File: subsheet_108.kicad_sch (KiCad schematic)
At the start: 15 parts

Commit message: fini eprom, réarrange la feuille, version alpha
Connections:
- net ~{CS_EPROM}: now reaches I14.4 (1Y3), I14.5 (1Y2), R30.2
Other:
- note added: "Vers I04"
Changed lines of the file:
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@@
     (title "Conversion du Thomson MO5 — Unité centrale v1")
     (date "2023-05-24")
-    (rev "DRAFT")
+    (rev "ALPHA")
     (comment 1 "http://github.com/sporniket/kicad-conversions--thomson-mo5--v1")
     (comment 3 "Gate Array Motorola MCA 1300 ALS")
@@
   (junction (at 151.13 167.64) (diameter 0) (color 0 0 0 0)
   )
+  (junction (at 52.07 147.32) (diameter 0) (color 0 0 0 0)
+  )
   (junction (at 93.98 190.5) (diameter 0) (color 0 0 0 0)
   )
@@
     (stroke (width 0) (type default) (color 0 0 0 0))
   )
+  (wire (pts (xy 49.53 147.32) (xy 52.07 147.32))
+    (stroke (width 0) (type default) (color 0 0 0 0))
+  )
   (wire (pts (xy 93.98 68.58) (xy 109.22 68.58))
     (stroke (width 0) (type default) (color 0 0 0 0))
+  )
+  (text "Vers I04" (at 36.83 148.59 180)
+    (effects (font (size 1.27 1.27)) (justify right bottom))
   )
   (label "A15" (at 80.01 129.54 0)
@@
       (effects (font (size 1.27 1.27)) (justify right) hide)
     )
+  )
+  (global_label "~{CS_EPROM}" (shape output) (at 49.53 147.32 180) (fields_autoplaced)
+    (effects (font (size 1.27 1.27)) (justify right))
+    (property "Intersheet References" "${INTERSHEET_REFS}" (id 0) (at 37.1988 147.2406 0)
+      (effects (font (size 1.27 1.27)) (justify right) hide)
+    )

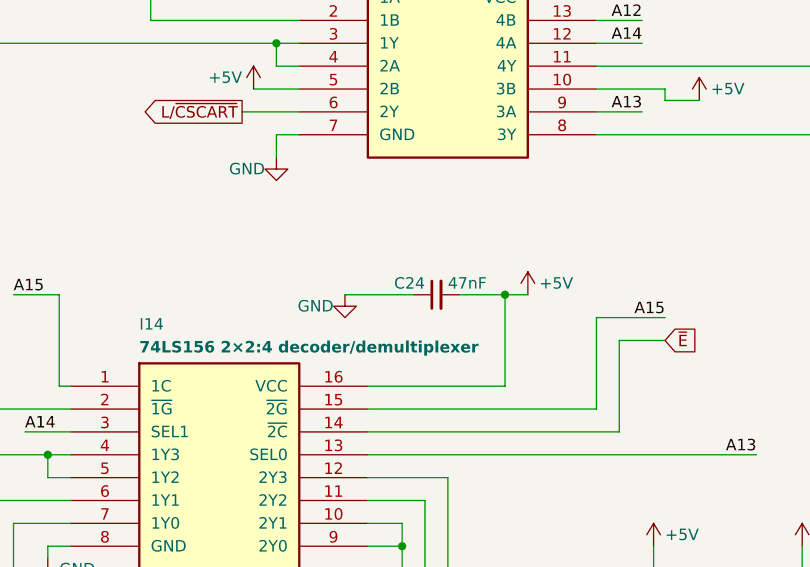
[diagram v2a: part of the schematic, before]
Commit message: fixes DRC : duplicate, designators with '?'
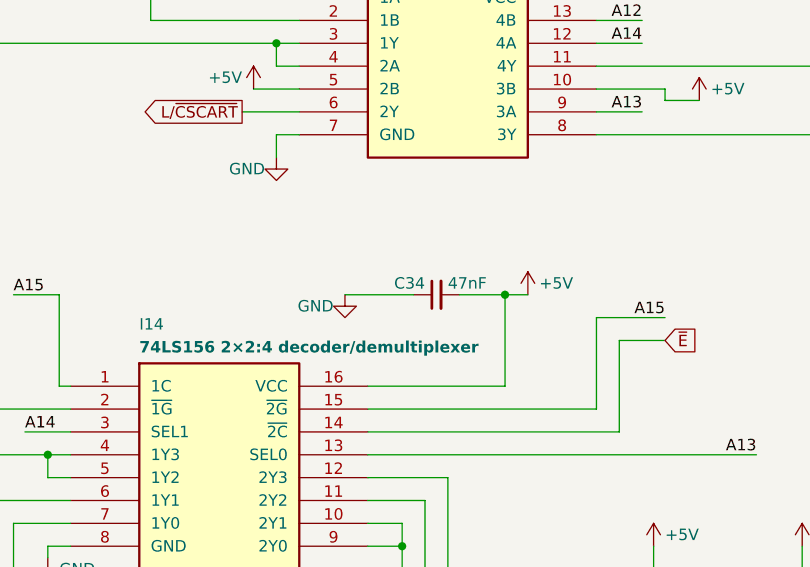
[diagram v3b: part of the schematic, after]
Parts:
- renumbered C24 to C34
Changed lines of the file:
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@@
   (symbol (lib_id "power:+5V") (at 69.85 205.74 0) (unit 1)
     (in_bom yes) (on_board yes)
-    (property "Reference" "#PWR?" (id 0) (at 69.85 209.55 0)
+    (property "Reference" "#PWR0120" (id 0) (at 69.85 209.55 0)
       (effects (font (size 1.27 1.27)) hide)
     )
@@
   (symbol (lib_id "power:GND") (at 58.42 76.2 0) (unit 1)
     (in_bom yes) (on_board yes)
-    (property "Reference" "#PWR?" (id 0) (at 58.42 82.55 0)
+    (property "Reference" "#PWR0131" (id 0) (at 58.42 82.55 0)
       (effects (font (size 1.27 1.27)) hide)
     )
@@
   (symbol (lib_id "Device:C_Small") (at 127 129.54 90) (unit 1)
     (in_bom yes) (on_board yes)
-    (property "Reference" "C24" (id 0) (at 125.73 128.27 90)
+    (property "Reference" "C34" (id 0) (at 125.73 128.27 90)
       (effects (font (size 1.27 1.27)) (justify left))
     )
@@
   (symbol (lib_id "power:+5V") (at 156.21 86.36 0) (unit 1)
     (in_bom yes) (on_board yes)
-    (property "Reference" "#PWR?" (id 0) (at 156.21 90.17 0)
+    (property "Reference" "#PWR0123" (id 0) (at 156.21 90.17 0)
       (effects (font (size 1.27 1.27)) hide)
     )
@@
   (symbol (lib_id "power:GND") (at 104.14 233.68 0) (unit 1)
     (in_bom yes) (on_board yes)
-    (property "Reference" "#PWR?" (id 0) (at 104.14 240.03 0)
+    (property "Reference" "#PWR0121" (id 0) (at 104.14 240.03 0)
       (effects (font (size 1.27 1.27)) hide)
     )
@@
   (symbol (lib_id "power:GND") (at 109.22 114.3 0) (unit 1)
     (in_bom yes) (on_board yes)
-    (property "Reference" "#PWR?" (id 0) (at 109.22 120.65 0)
+    (property "Reference" "#PWR0129" (id 0) (at 109.22 120.65 0)
       (effects (font (size 1.27 1.27)) hide)
     )
@@
   (symbol (lib_id "power:+5V") (at 106.68 106.68 0) (unit 1)
     (in_bom yes) (on_board yes)
-    (property "Reference" "#PWR?" (id 0) (at 106.68 110.49 0)
+    (property "Reference" "#PWR0119" (id 0) (at 106.68 110.49 0)
       (effects (font (size 1.27 1.27)) hide)
     )
@@
   (symbol (lib_id "power:GND") (at 116.84 129.54 0) (unit 1)
     (in_bom yes) (on_board yes)
-    (property "Reference" "#PWR?" (id 0) (at 116.84 135.89 0)
+    (property "Reference" "#PWR0130" (id 0) (at 116.84 135.89 0)
       (effects (font (size 1.27 1.27)) hide)
     )
@@
   (symbol (lib_id "power:+5V") (at 52.07 139.7 0) (unit 1)
     (in_bom yes) (on_board yes)
-    (property "Reference" "#PWR?" (id 0) (at 52.07 143.51 0)
+    (property "Reference" "#PWR0118" (id 0) (at 52.07 143.51 0)
       (effects (font (size 1.27 1.27)) hide)
     )
@@
   (symbol (lib_id "power:GND") (at 83.82 48.26 0) (unit 1)
     (in_bom yes) (on_board yes)
-    (property "Reference" "#PWR?" (id 0) (at 83.82 54.61 0)
+    (property "Reference" "#PWR0132" (id 0) (at 83.82 54.61 0)
       (effects (font (size 1.27 1.27)) hide)
     )
@@
   (symbol (lib_id "power:GND") (at 148.59 205.74 0) (unit 1)
     (in_bom yes) (on_board yes)
-    (property "Reference" "#PWR?" (id 0) (at 148.59 212.09 0)
+    (property "Reference" "#PWR0122" (id 0) (at 148.59 212.09 0)
       (effects (font (size 1.27 1.27)) hide)
     )
@@
   (symbol (lib_id "power:GND") (at 109.22 77.47 0) (unit 1)
     (in_bom yes) (on_board yes)
-    (property "Reference" "#PWR?" (id 0) (at 109.22 83.82 0)
+    (property "Reference" "#PWR0126" (id 0) (at 109.22 83.82 0)
       (effects (font (size 1.27 1.27)) hide)
     )
@@
   (symbol (lib_id "power:GND") (at 49.53 205.74 0) (unit 1)
     (in_bom yes) (on_board yes)
-    (property "Reference" "#PWR?" (id 0) (at 49.53 212.09 0)
+    (property "Reference" "#PWR0136" (id 0) (at 49.53 212.09 0)
       (effects (font (size 1.27 1.27)) hide)
     )
@@
   (symbol (lib_id "power:+5V") (at 104.14 48.26 0) (unit 1)
     (in_bom yes) (on_board yes)
-    (property "Reference" "#PWR?" (id 0) (at 104.14 52.07 0)
+    (property "Reference" "#PWR0127" (id 0) (at 104.14 52.07 0)
       (effects (font (size 1.27 1.27)) hide)
     )
@@
   (symbol (lib_id "power:GND") (at 135.89 86.36 0) (unit 1)
     (in_bom yes) (on_board yes)
-    (property "Reference" "#PWR?" (id 0) (at 135.89 92.71 0)
+    (property "Reference" "#PWR0125" (id 0) (at 135.89 92.71 0)
       (effects (font (size 1.27 1.27)) hide)
     )
@@
   (symbol (lib_id "power:GND") (at 27.94 233.68 0) (unit 1)
     (in_bom yes) (on_board yes)
-    (property "Reference" "#PWR?" (id 0) (at 27.94 240.03 0)
+    (property "Reference" "#PWR0135" (id 0) (at 27.94 240.03 0)
       (effects (font (size 1.27 1.27)) hide)
     )
@@
   (symbol (lib_id "power:+5V") (at 137.16 129.54 0) (unit 1)
     (in_bom yes) (on_board yes)
-    (property "Reference" "#PWR?" (id 0) (at 137.16 133.35 0)
+    (property "Reference" "#PWR0128" (id 0) (at 137.16 133.35 0)
       (effects (font (size 1.27 1.27)) hide)
     )
@@
   (symbol (lib_id "power:+5V") (at 167.64 157.48 0) (unit 1)
     (in_bom yes) (on_board yes)
-    (property "Reference" "#PWR?" (id 0) (at 167.64 161.29 0)
+    (property "Reference" "#PWR0139" (id 0) (at 167.64 161.29 0)
       (effects (font (size 1.27 1.27)) hide)
     )
@@
   (symbol (lib_id "power:+5V") (at 128.27 205.74 0) (unit 1)
     (in_bom yes) (on_board yes)
-    (property "Reference" "#PWR?" (id 0) (at 128.27 209.55 0)
+    (property "Reference" "#PWR0137" (id 0) (at 128.27 209.55 0)
       (effects (font (size 1.27 1.27)) hide)
     )
@@
   (symbol (lib_id "power:GND") (at 83.82 158.75 0) (unit 1)
     (in_bom yes) (on_board yes)
-    (property "Reference" "#PWR?" (id 0) (at 83.82 165.1 0)
+    (property "Reference" "#PWR0134" (id 0) (at 83.82 165.1 0)
       (effects (font (size 1.27 1.27)) hide)
     )
@@
   (symbol (lib_id "power:+5V") (at 156.21 107.95 0) (unit 1)
     (in_bom yes) (on_board yes)
-    (property "Reference" "#PWR?" (id 0) (at 156.21 111.76 0)
+    (property "Reference" "#PWR0124" (id 0) (at 156.21 111.76 0)
       (effects (font (size 1.27 1.27)) hide)
     )
@@
   (symbol (lib_id "power:+5V") (at 67.31 162.56 0) (unit 1)
     (in_bom yes) (on_board yes)
-    (property "Reference" "#PWR?" (id 0) (at 67.31 166.37 0)
+    (property "Reference" "#PWR0133" (id 0) (at 67.31 166.37 0)
       (effects (font (size 1.27 1.27)) hide)
     )
@@
   (symbol (lib_id "power:+5V") (at 151.13 157.48 0) (unit 1)
     (in_bom yes) (on_board yes)
-    (property "Reference" "#PWR?" (id 0) (at 151.13 161.29 0)
-      (effects (font (size 1.27 1.27)) hide)
-    )
+    (property "Reference" "#PWR0138" (id 0) (at 151.13 161.29 0)
+      (effects (font (size 1.27 1.27)) hide)
+    )

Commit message: start association symbols-footprints
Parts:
- C34, C45, C46, C48, C49: footprint (none) -> commons-passives_THT:Passive_THT_capacitor_mlcc_W2.54mm_L5.08mm
- R30, R31, R32, R33, R36: footprint (none) -> commons-passives_THT:Passive_THT_resistor_EU_W2.54mm_L12.70mm
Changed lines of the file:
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@@
       (effects (font (size 1.27 1.27)) (justify right))
     )
-    (property "Footprint" "" (id 2) (at 138.43 205.74 0)
+    (property "Footprint" "commons-passives_THT:Passive_THT_capacitor_mlcc_W2.54mm_L5.08mm" (id 2) (at 138.43 205.74 0)
       (effects (font (size 1.27 1.27)) hide)
     )
@@
       (effects (font (size 1.27 1.27)) (justify right))
     )
-    (property "Footprint" "" (id 2) (at 127 129.54 0)
+    (property "Footprint" "commons-passives_THT:Passive_THT_capacitor_mlcc_W2.54mm_L5.08mm" (id 2) (at 127 129.54 0)
       (effects (font (size 1.27 1.27)) hide)
     )
@@
       (effects (font (size 1.27 1.27)) (justify left))
     )
-    (property "Footprint" "" (id 2) (at 67.31 166.37 0)
+    (property "Footprint" "commons-passives_THT:Passive_THT_resistor_EU_W2.54mm_L12.70mm" (id 2) (at 67.31 166.37 0)
       (effects (font (size 1.27 1.27)) hide)
     )
@@
       (effects (font (size 1.27 1.27)) (justify left))
     )
-    (property "Footprint" "" (id 2) (at 151.13 162.56 0)
+    (property "Footprint" "commons-passives_THT:Passive_THT_resistor_EU_W2.54mm_L12.70mm" (id 2) (at 151.13 162.56 0)
       (effects (font (size 1.27 1.27)) hide)
     )
@@
       (effects (font (size 1.27 1.27)) (justify right))
     )
-    (property "Footprint" "" (id 2) (at 146.05 86.36 0)
+    (property "Footprint" "commons-passives_THT:Passive_THT_capacitor_mlcc_W2.54mm_L5.08mm" (id 2) (at 146.05 86.36 0)
       (effects (font (size 1.27 1.27)) hide)
     )
@@
       (effects (font (size 1.27 1.27)) (justify left))
     )
-    (property "Footprint" "" (id 2) (at 52.07 143.51 0)
+    (property "Footprint" "commons-passives_THT:Passive_THT_resistor_EU_W2.54mm_L12.70mm" (id 2) (at 52.07 143.51 0)
       (effects (font (size 1.27 1.27)) hide)
     )
@@
       (effects (font (size 1.27 1.27)) (justify left))
     )
-    (property "Footprint" "" (id 2) (at 109.22 72.39 0)
+    (property "Footprint" "commons-passives_THT:Passive_THT_resistor_EU_W2.54mm_L12.70mm" (id 2) (at 109.22 72.39 0)
       (effects (font (size 1.27 1.27)) hide)
     )
@@
       (effects (font (size 1.27 1.27)) (justify right))
     )
-    (property "Footprint" "" (id 2) (at 59.69 205.74 0)
+    (property "Footprint" "commons-passives_THT:Passive_THT_capacitor_mlcc_W2.54mm_L5.08mm" (id 2) (at 59.69 205.74 0)
       (effects (font (size 1.27 1.27)) hide)
     )
@@
       (effects (font (size 1.27 1.27)) (justify left))
     )
-    (property "Footprint" "" (id 2) (at 167.64 162.56 0)
+    (property "Footprint" "commons-passives_THT:Passive_THT_resistor_EU_W2.54mm_L12.70mm" (id 2) (at 167.64 162.56 0)
       (effects (font (size 1.27 1.27)) hide)
     )
@@
       (effects (font (size 1.27 1.27)) (justify right))
     )
-    (property "Footprint" "" (id 2) (at 93.98 48.26 0)
-      (effects (font (size 1.27 1.27)) hide)
-    )
+    (property "Footprint" "commons-passives_THT:Passive_THT_capacitor_mlcc_W2.54mm_L5.08mm" (id 2) (at 93.98 48.26 0)
+      (effects (font (size 1.27 1.27)) hide)
+    )
